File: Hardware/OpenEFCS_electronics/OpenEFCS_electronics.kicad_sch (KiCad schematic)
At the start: 69 parts, among them J1 15v, J2 GND, J3 M+, J4 M-, J5 CTRL-B, J6 PGRM, J7 CTRL-F, Q1 DMG3402L, Q2 BSC010N04LS6, Q3 BSC010N04LS6, SW1 DECOCK, U1 STM32F042K4Tx, U2 AP1117-33, U3 AOZ1282CI-1, U4 XJNG2103, U5 INA2180A4, Y1 8MHz 12pF

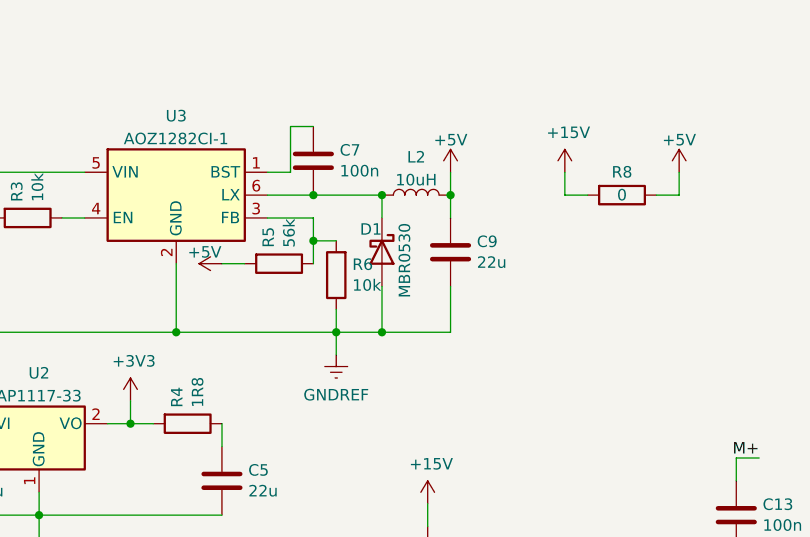
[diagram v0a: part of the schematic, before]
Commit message: Updated minor BOM mistake
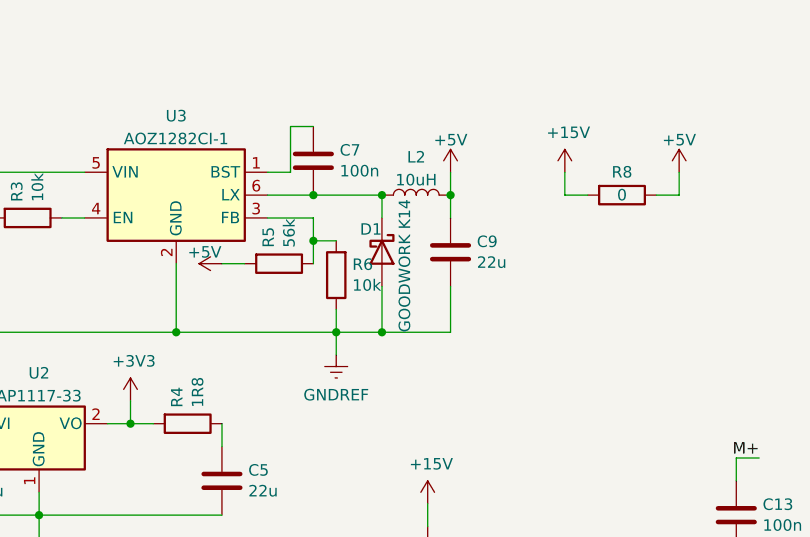
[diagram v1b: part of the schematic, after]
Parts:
- D1: value MBR0530 -> GOODWORK K14
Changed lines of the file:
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@@
       (effects (font (size 1.27 1.27)) (justify right))
     )
-    (property "Value" "MBR0530" (id 1) (at 96.52 43.18 0)
+    (property "Value" "GOODWORK K14" (id 1) (at 96.52 46.99 0)
       (effects (font (size 1.27 1.27)) (justify right))
     )
@@
       (effects (font (size 1.27 1.27)) hide)
     )
-    (property "Datasheet" "http://www.mccsemi.com/up_pdf/MBR0520~MBR0580(SOD123).pdf" (id 3) (at 93.98 38.1 0)
+    (property "Datasheet" "https://datasheet.lcsc.com/lcsc/2012311737_GOODWORK-K14_C908662.pdf" (id 3) (at 93.98 38.1 0)
       (effects (font (size 1.27 1.27)) hide)
     )
@@
     )
     (path "/c96401dc-79d2-476c-9dbb-82fe95d90cf1"
-      (reference "D1") (unit 1) (value "MBR0530") (footprint "Diode_SMD:D_SOD-123")
+      (reference "D1") (unit 1) (value "GOODWORK K14") (footprint "Diode_SMD:D_SOD-123")
     )
     (path "/00000000-0000-0000-0000-000062b2f603"

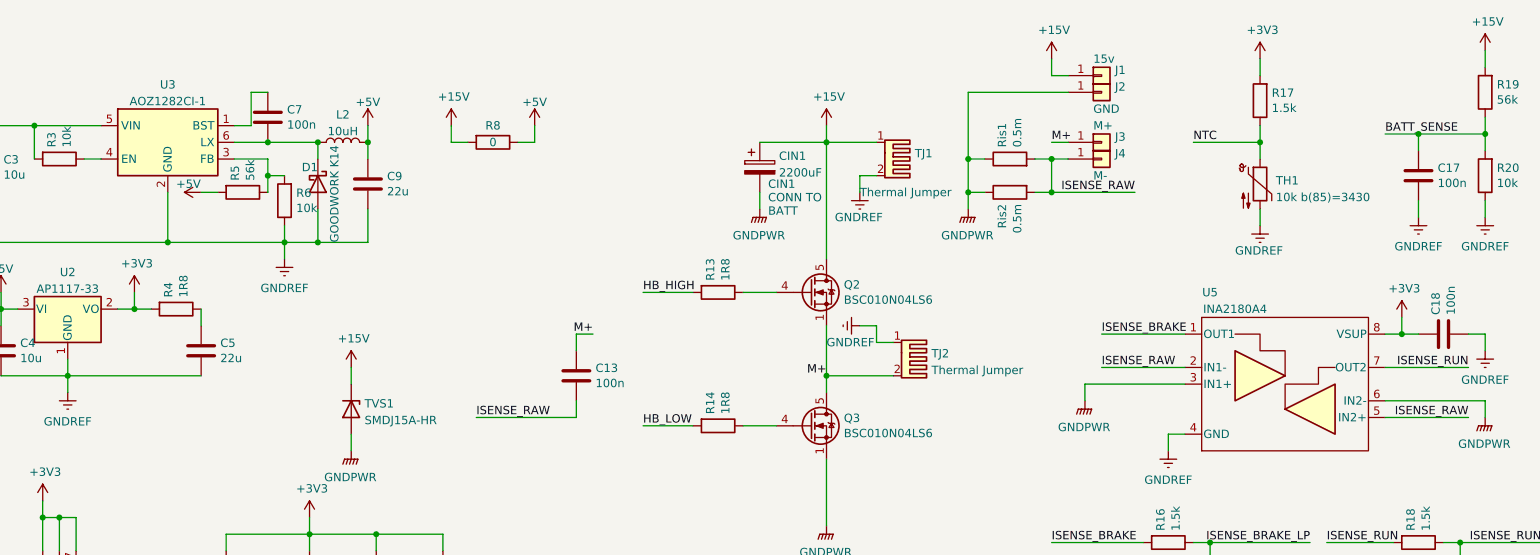
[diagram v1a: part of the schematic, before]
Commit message: Release v0.3.1
Corrected footprint for INA2180
Regenerated manufacturing files
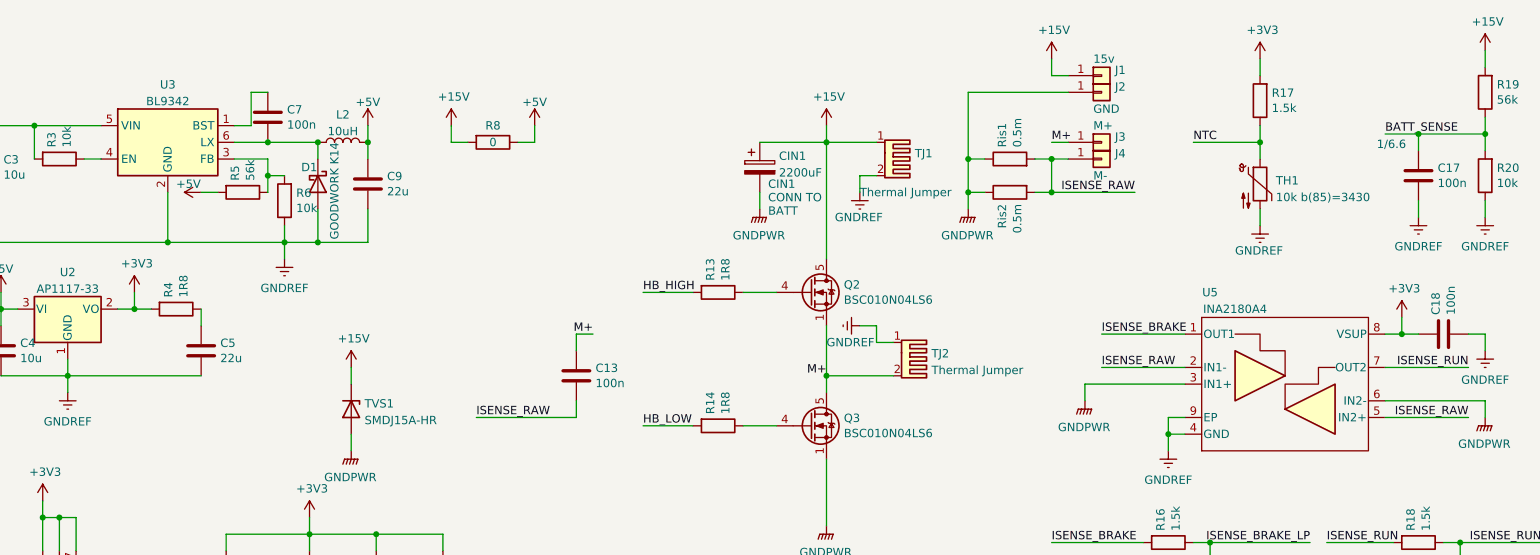
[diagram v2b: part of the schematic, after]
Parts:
- U3: value AOZ1282CI-1 -> BL9342
- U5: footprint Package_DFN_QFN:OnSemi_DFN-8_2x2mm_P0.5mm -> Package_DFN_QFN:DFN-8-1EP_2x2mm_P0.5mm_EP0.9x1.6mm
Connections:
- net GNDREF: now also U5.9 (EP)
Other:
- note added: "1/6.6"
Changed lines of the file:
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@@
   (junction (at 259.08 60.96) (diameter 0) (color 0 0 0 0)
   )
+  (junction (at 223.52 76.2) (diameter 0) (color 0 0 0 0)
+  )
   (junction (at 189.23 115.57) (diameter 0) (color 0 0 0 0)
   )
@@
     (stroke (width 0) (type default) (color 0 0 0 0))
   )
+  (wire (pts (xy 223.52 76.2) (xy 223.52 73.66))
+    (stroke (width 0) (type default) (color 0 0 0 0))
+  )
   (wire (pts (xy 196.85 135.89) (xy 207.01 135.89))
     (stroke (width 0) (type default) (color 0 0 0 0))
@@
     (stroke (width 0) (type default) (color 0 0 0 0))
   )
+  (wire (pts (xy 223.52 73.66) (xy 226.06 73.66))
+    (stroke (width 0) (type default) (color 0 0 0 0))
+  )
   (wire (pts (xy 111.76 172.72) (xy 111.76 175.26))
     (stroke (width 0) (type default) (color 0 0 0 0))
@@
     (effects (font (size 1.27 1.27)) (justify left bottom))
   )
+  (text "1/6.6" (at 255.27 33.02 0)
+    (effects (font (size 1.27 1.27)) (justify left bottom))
+  )
   (text "CIN1\nCONN TO\nBATT" (at 162.56 43.18 0)
     (effects (font (size 1.27 1.27)) (justify left bottom))
@@
     (in_bom yes) (on_board yes) (fields_autoplaced)
     (property "Reference" "U3" (id 0) (at 71.12 22.9702 0))
-    (property "Value" "AOZ1282CI-1" (id 1) (at 71.12 25.5071 0))
+    (property "Value" "BL9342" (id 1) (at 71.12 25.5071 0))
     (property "Footprint" "Package_TO_SOT_SMD:SOT-23-6" (id 2) (at 88.9 38.1 0)
       (effects (font (size 1.27 1.27)) hide)
     )
-    (property "Datasheet" "http://www.aosmd.com/res/data_sheets/AOZ1282CI-1.pdf" (id 3) (at 64.77 38.1 0)
+    (property "Datasheet" "https://datasheet.lcsc.com/lcsc/1809050135_BL-Shanghai-Belling-BL9342_C93176.pdf" (id 3) (at 64.77 38.1 0)
       (effects (font (size 1.27 1.27)) hide)
     )
@@
     (pin "2")
   )
+  (symbol (lib_id "Diode:MBR0530") (at 93.98 38.1 270) (unit 1)
+    (in_bom yes) (on_board yes)
+    (property "Reference" "D1" (id 0) (at 91.44 35.56 90)
+      (effects (font (size 1.27 1.27)) (justify left))
+    )
+    (property "Value" "GOODWORK K14" (id 1) (at 96.52 31.75 0)
+      (effects (font (size 1.27 1.27)) (justify left))
+    )
+    (property "Footprint" "Diode_SMD:D_SOD-123" (id 2) (at 89.535 38.1 0)
+      (effects (font (size 1.27 1.27)) hide)
+    )
+    (property "Datasheet" "https://datasheet.lcsc.com/lcsc/2012311737_GOODWORK-K14_C908662.pdf" (id 3) (at 93.98 38.1 0)
+      (effects (font (size 1.27 1.27)) hide)
+    )
+    (pin "1")
+    (pin "2")
+  )
   (symbol (lib_id "power:GNDREF") (at 229.87 105.41 0) (unit 1)
     (in_bom yes) (on_board yes) (fields_autoplaced)
@@
     (property "Reference" "U5" (id 0) (at 229.87 54.61 0))
     (property "Value" "INA2180A4" (id 1) (at 233.68 57.15 0))
-    (property "Footprint" "Package_DFN_QFN:OnSemi_DFN-8_2x2mm_P0.5mm" (id 2) (at 236.22 66.04 0)
+    (property "Footprint" "Package_DFN_QFN:DFN-8-1EP_2x2mm_P0.5mm_EP0.9x1.6mm" (id 2) (at 236.22 66.04 0)
       (effects (font (size 1.27 1.27)) hide)
     )
@@
     (pin "7")
     (pin "8")
+    (pin "9")
   )
   (symbol (lib_id "power:GNDREF") (at 55.88 69.85 0) (unit 1)
@@
     (pin "1")
   )
-  (symbol (lib_id "Diode:MBR0530") (at 93.98 38.1 270) (unit 1)
-    (in_bom yes) (on_board yes)
-    (property "Reference" "D1" (id 0) (at 93.98 35.56 90)
-      (effects (font (size 1.27 1.27)) (justify right))
-    )
-    (property "Value" "GOODWORK K14" (id 1) (at 96.52 46.99 0)
-      (effects (font (size 1.27 1.27)) (justify right))
-    )
-    (property "Footprint" "Diode_SMD:D_SOD-123" (id 2) (at 89.535 38.1 0)
-      (effects (font (size 1.27 1.27)) hide)
-    )
-    (property "Datasheet" "https://datasheet.lcsc.com/lcsc/2012311737_GOODWORK-K14_C908662.pdf" (id 3) (at 93.98 38.1 0)
-      (effects (font (size 1.27 1.27)) hide)
-    )
-    (pin "1")
-    (pin "2")
-  )
   (symbol (lib_id "Device:C") (at 229.87 99.06 0) (unit 1)
     (in_bom yes) (on_board yes)
@@
       (reference "CIN1") (unit 1) (value "2200uF") (footprint "")
     )
-    (path "/c96401dc-79d2-476c-9dbb-82fe95d90cf1"
+    (path "/842e7979-a976-4b0c-af33-d6c4e33067eb"
       (reference "D1") (unit 1) (value "GOODWORK K14") (footprint "Diode_SMD:D_SOD-123")
     )
@@
     )
     (path "/3b1687b5-befb-41bd-a538-d2e81ac558fd"
-      (reference "U3") (unit 1) (value "AOZ1282CI-1") (footprint "Package_TO_SOT_SMD:SOT-23-6")
+      (reference "U3") (unit 1) (value "BL9342") (footprint "Package_TO_SOT_SMD:SOT-23-6")
     )
     (path "/9e2f1b5a-a843-4e32-8d4a-b0eed571e9ba"
@@
     )
     (path "/8a08d194-2181-4a4f-ad94-8bd125942a69"
-      (reference "U5") (unit 1) (value "INA2180A4") (footprint "Package_DFN_QFN:OnSemi_DFN-8_2x2mm_P0.5mm")
+      (reference "U5") (unit 1) (value "INA2180A4") (footprint "Package_DFN_QFN:DFN-8-1EP_2x2mm_P0.5mm_EP0.9x1.6mm")
     )
     (path "/00000000-0000-0000-0000-000062c7c004"

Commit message: design complete for second prototype
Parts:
- removed C12: 4.7u, Capacitor_SMD:C_0402_1005Metric, symbol Device:C
- removed C16: 100n, Capacitor_SMD:C_0402_1005Metric, symbol Device:C
- removed C4: 10u, Capacitor_SMD:C_0603_1608Metric, symbol Device:C
- removed J6: PGRM, Connector_PinHeader_2.54mm:PinHeader_2x05_P2.54mm_Vertical, symbol Connector_Generic:Conn_02x05_Odd_Even
- removed J7: CTRL-F, Connector_JST:JST_GH_BM08B-GHS-TBT_1x08-1MP_P1.25mm_Vertical, symbol Connector_Generic_MountingPin:Conn_01x08_MountingPin
- removed R4: 1R8, Resistor_SMD:R_0603_1608Metric, symbol Device:R
- removed Ris1, Ris2: 0.5m, Resistor_SMD:R_1206_3216Metric, symbol Device:R
- removed TJ2: Thermal Jumper, Resistor_SMD:R_1206_3216Metric, symbol Mechanical:Heatsink_Pad_2Pin
- removed TVS1: SMDJ15A-HR, Diode_SMD:D_SMC, symbol Device:D_Zener
- removed U2: AP1117-33, Package_TO_SOT_SMD:SOT-223-3_TabPin2, symbol Regulator_Linear:AP1117-33
- removed U5: INA2180A4, Package_DFN_QFN:DFN-8-1EP_2x2mm_P0.5mm_EP0.9x1.6mm, symbol pspice:OPAMP
- removed Y1: 8MHz 12pF, Crystal:Crystal_SMD_3225-4Pin_3.2x2.5mm, symbol Device:Crystal_GND24
- added C13, C15: 10u, Capacitor_SMD:C_0805_2012Metric, symbol Device:C
- added C3, C7: 100n, Capacitor_SMD:C_0603_1608Metric, symbol Device:C
- added CIN1: 22uF, Capacitor_Tantalum_SMD:CP_EIA-3528-12_Kemet-T, symbol Device:C_Polarized
- added D4: YLW, LED_SMD:LED_0603_1608Metric, symbol Device:LED
- added F1: 3557, KiCAD-Custom-Lib:Keystone 3557, symbol Device:Fuse
- added JP1: BYP, Jumper:SolderJumper-2_P1.3mm_Open_TrianglePad1.0x1.5mm, symbol Jumper:SolderJumper_2_Open
- added R17, R3, R7: 10k, Resistor_SMD:R_0603_1608Metric, symbol Device:R
- added SW1: PREC, Button_Switch_SMD:SW_SPST_B3U-1000P, symbol Switch:SW_SPST
- added TP1: NTC, TestPoint:TestPoint_Pad_1.0x1.0mm, symbol Connector:TestPoint
- added TP10: BVS, TestPoint:TestPoint_Pad_1.0x1.0mm, symbol Connector:TestPoint
- added TP11: ISF, TestPoint:TestPoint_Pad_1.0x1.0mm, symbol Connector:TestPoint
- added TP2: PML, TestPoint:TestPoint_Pad_1.0x1.0mm, symbol Connector:TestPoint
- added TP3: PMH, TestPoint:TestPoint_Pad_1.0x1.0mm, symbol Connector:TestPoint
- added TP4: TRC, TestPoint:TestPoint_Pad_1.0x1.0mm, symbol Connector:TestPoint
- added TP5: ISR, TestPoint:TestPoint_Pad_1.0x1.0mm, symbol Connector:TestPoint
- added TP6: SIO, TestPoint:TestPoint_Pad_1.0x1.0mm, symbol Connector:TestPoint
- added TP7: B0, TestPoint:TestPoint_Pad_1.0x1.0mm, symbol Connector:TestPoint
- added TP8: RST, TestPoint:TestPoint_Pad_1.0x1.0mm, symbol Connector:TestPoint
- added TP9: SCK, TestPoint:TestPoint_Pad_1.0x1.0mm, symbol Connector:TestPoint
- added U2: AP2204K-3.3, Package_TO_SOT_SMD:SOT-23-5, symbol Regulator_Linear:AP2204K-3.3
- added U5: INA194, Package_TO_SOT_SMD:SOT-23-5, symbol Amplifier_Current:INA194
- C1, C18, C6: footprint Capacitor_SMD:C_0402_1005Metric -> Capacitor_SMD:C_0603_1608Metric
- C10: renamed from C9; value 22u -> 10u; footprint Capacitor_SMD:C_0603_1608Metric -> Capacitor_SMD:C_0805_2012Metric
- C11: renamed from C10; footprint Capacitor_SMD:C_0402_1005Metric -> Capacitor_SMD:C_0603_1608Metric
- C12: renamed from C11; footprint Capacitor_SMD:C_0402_1005Metric -> Capacitor_SMD:C_0603_1608Metric
- C14: renamed from C13; footprint Capacitor_SMD:C_0402_1005Metric -> Capacitor_SMD:C_0603_1608Metric
- C16: renamed from C14; footprint Capacitor_SMD:C_0603_1608Metric -> Capacitor_SMD:C_0805_2012Metric
- C17: renamed from C15; footprint Capacitor_SMD:C_0603_1608Metric -> Capacitor_SMD:C_0805_2012Metric
- C19: renamed from C17; footprint Capacitor_SMD:C_0402_1005Metric -> Capacitor_SMD:C_0603_1608Metric
- C2: footprint Capacitor_SMD:C_0603_1608Metric -> Capacitor_SMD:C_0805_2012Metric
- C20: renamed from C19; footprint Capacitor_SMD:C_0402_1005Metric -> Capacitor_SMD:C_0603_1608Metric
- C4: renamed from C3; footprint Capacitor_SMD:C_0603_1608Metric -> Capacitor_SMD:C_0805_2012Metric
- C5: value 22u -> 10u; footprint Capacitor_SMD:C_0603_1608Metric -> Capacitor_SMD:C_0805_2012Metric; now left out of the parts list
- C8: renamed from C7; footprint Capacitor_SMD:C_0402_1005Metric -> Capacitor_SMD:C_0603_1608Metric
- C9: renamed from C8; footprint Capacitor_SMD:C_0402_1005Metric -> Capacitor_SMD:C_0603_1608Metric
- J1, J2, J3, J4: now left out of the parts list
- J5: value CTRL-B -> CTRL; footprint Connector_PinHeader_2.00mm:PinHeader_1x08_P2.00mm_Vertical -> Connector_JST:JST_PH_B8B-PH-K_1x08_P2.00mm_Vertical
- L1, L2: value 10uH -> 6.8uH
- R10: renamed from R9; footprint Resistor_SMD:R_0402_1005Metric -> Resistor_SMD:R_0603_1608Metric
- R11: renamed from R10; footprint Resistor_SMD:R_0402_1005Metric -> Resistor_SMD:R_0603_1608Metric
- R12: renamed from R11; footprint Resistor_SMD:R_0402_1005Metric -> Resistor_SMD:R_0603_1608Metric
- R13: renamed from R12; footprint Resistor_SMD:R_0402_1005Metric -> Resistor_SMD:R_0603_1608Metric
- R16, R5, R6: footprint Resistor_SMD:R_0402_1005Metric -> Resistor_SMD:R_0603_1608Metric
- R19: renamed from R17; footprint Resistor_SMD:R_0402_1005Metric -> Resistor_SMD:R_0603_1608Metric
- R2: value 10k -> 56k; footprint Resistor_SMD:R_0402_1005Metric -> Resistor_SMD:R_0603_1608Metric
- R20: renamed from R18; footprint Resistor_SMD:R_0402_1005Metric -> Resistor_SMD:R_0603_1608Metric
- R21: renamed from R19; footprint Resistor_SMD:R_0402_1005Metric -> Resistor_SMD:R_0603_1608Metric
- R22: renamed from R20; footprint Resistor_SMD:R_0402_1005Metric -> Resistor_SMD:R_0603_1608Metric
- R4: renamed from R3; footprint Resistor_SMD:R_0402_1005Metric -> Resistor_SMD:R_0603_1608Metric
- R8: value 0 -> 56k
- R9: renamed from R7; footprint Resistor_SMD:R_0402_1005Metric -> Resistor_SMD:R_0603_1608Metric
- SW2: renamed from SW1; value DECOCK -> CONF; footprint Button_Switch_SMD:SW_SPST_B3U-3000P -> Button_Switch_SMD:SW_SPST_B3U-1000P
- TJ1: value Thermal Jumper -> ThermJmpr
- renumbered CIN1 to CIN2, D4 to D5, R13 to R14, R14 to R15, R15 to R18
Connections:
- net ISENSE_RAW is gone; now on net GNDPWR: C14.2, J4.1 (Pin_1)
- net OSCIN is gone; now on net CONF: U1.2 (PF0)
- net Tx is gone; now on net LED1: U1.19 (PA9)
- net +15V: now also C15.1, D4.1 (K), F1.1, JP1.1 (A), R17.2, U5.3 (+); no longer J1.1 (Pin_1), R8.2
- net +3V3: now also C18.2, C13.1, R3.2, R7.2, U2.5 (VOUT), U5.5 (V+); no longer C18.1
- net +5V: now also C5.1, JP1.2 (B), U2.1 (VIN), U2.3 (EN); no longer R8.1
- net AIN1: now also C3.1, R3.1
- net BATT_SENSE: now also TP10.1
- net BOOT0: now also R8.2, TP7.1
- net GNDPWR: now also C15.2, CIN1.2
- net GNDREF: now also C18.1, R8.1, C13.2, C3.2, C7.2, R17.1, SW1.1 (A), U2.2 (GND), U5.2 (GND); no longer C18.2
- net ISENSE_RUN: now also TP5.1, U5.1
- net ISENSE_RUN_LP: now also U1.13 (PA7), TP11.1; no longer U1.10 (PA4)
- net LED1: no longer U1.21 (PA11)
- net M+: now also U5.4 (-)
- net NTC: now also U1.14 (PB0), TP1.1; no longer U1.13 (PA7)
- net RESET: now also TP8.1
- net SWCLK: now also TP9.1
- net SWDIO: now also TP6.1
- net Tracer: now also TP4.1
- net DECOCK renamed CONF
- net CONF: no longer U1.22 (PA12)
- net ISENSE_BRAKE: no longer names the net of R16.2
- net ISENSE_BRAKE: now also D4.2 (A)
- net ISENSE_BRAKE_LP renamed +BATT
- net +BATT: now also J1.1 (Pin_1), CIN1.1, F1.2; no longer U1.11 (PA5)
- net OSCOUT: no longer names the net of U1.3 (PF1)
- net PWMMOT renamed PWML
- net PWML: now also TP2.1; no longer U4.2 (HIN)
- net Rx: no longer names the net of U1.20 (PA10)
- new net PREC: C7.1, R7.1, SW1.2 (B), U1.10 (PA4)
- new net PWMH: TP3.1, U1.11 (PA5), U4.2 (HIN)
- no-connect marks 6 -> 5
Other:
- note added: "All schottky compatible with all other schottky rated >25V >300mA"
- note added: "Also suitable with LKS560 3s-4s SLM2009 3s-4s"
- note added: "Can also use ME3116 - C7 use 820nF AOZ1282CI-1"
- note added: "Compatible with INA180A2"
- note added: "Compatible with most NOT ALL TDSON-8 MOSFETs"
- note added: "Compatible with, Without modification: STM32F051 STM32L072 STM32L051 Control UART Disabled: STM32F030 STM32F031 STM32L031"
- note added: "Designed for ??kHz PWM @ 4s ??kHz PWM @ 3s Bootstrap sync to gun cycle for const ON"
- note added: "Fuse: Cased such as 3557-2 Recommanded"
- note added: "If Buck DNP Bridge JP If Buck is Present DO NOT BRIDGE"
- note added: "LC 2nd Odr Low Pass 16kHz"
- title: OpenEFCS Electronics v0.3 -> OpenEFCS Electronics v0.4
- moved on the sheet: C18, C20, J1, J2, J3, J4, J5, R20
